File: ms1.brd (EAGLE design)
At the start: 160 x 100 mm, 145 parts, among them IC1 MAX3232EUE, IC2 MAX3380EEUP, J1 POWERPOLE_POWER25A, J10 Radio, J11 A3, J12 A4, J13 A5, J14 A6, J15 A7, J16 D1, J17 D2, J18 D3, J19 D4, J2 ON, J20 D5, J21 D6, J22 D7, J3 LED-EN, J4 RS232, J5 RS485, J6 A1, J7 I2C, J8 A2, J9 TTL_SERIAL, Q1 DMG6602SVT, Q2 DMG6602SVT, Q3 DMG6602SVT, Q4 DMG6602SVT, U1 LT1934ES6TRMPBF, U2 LT1934ES6TRMPBF, U3 DS3231SN, U4 ISL3179EIBZ, X1 KUSBVX-BS1N

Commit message: a little more routing
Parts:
- moved AGND 377.8 mm to (166.1, -11.8)
- moved BATV_B 276.8 mm to (63.8, 95.6)
- moved U$1 248.6 mm to (51.3, 80.5)
- moved U3 203.2 mm to (35.7, 59.9), flipped to the bottom, turned to 180 degrees
- moved U$4 42.3 mm to (124.8, 36.1)
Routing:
- net VBAT_B: track 0.00 -> 38.7 mm
- net GND: track 17.5 -> 17.6 mm, vias 3 -> 4

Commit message: power supplies mostly routed
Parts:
- moved Q4 253.2 mm to (111.5, 77.7), turned to 180 degrees
- moved R5 234.5 mm to (79.0, 92.8)
- moved L3 233.0 mm to (90.6, 87.5)
- moved C12 230.0 mm to (145.0, 83.9), turned to 270 degrees
- moved R31 223.4 mm to (149.5, 89.8), turned to 180 degrees
- moved 5V 222.3 mm to (149.9, 93.6)
- moved C11 216.4 mm to (127.6, 80.4), turned to 90 degrees
- moved R11 212.3 mm to (119.4, 80.9), turned to 180 degrees
- moved L6 207.7 mm to (143.3, 93.6)
- moved Q2 202.7 mm to (117.9, 84.6)
- moved R6 202.6 mm to (75.6, 89.3), turned to 90 degrees
- moved R9 200.8 mm to (116.5, 83.9), turned to 270 degrees
- moved U2 200.8 mm to (124.3, 88.3), turned to 270 degrees
- moved C8 200.1 mm to (121.2, 87.9), turned to 90 degrees
- moved R23 199.4 mm to (123.8, 94.0)
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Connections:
- net ADC_3V3 renamed VCC-3V
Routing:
- net SENSE_3V3: track 0.00 -> 298.2 mm, vias 0 -> 1
- net SENSE_5V: track 0.00 -> 275.8 mm
- net VCC: track 12.3 -> 148.3 mm
- net N$107: track 0.00 -> 39.8 mm
- net N$6: track 0.00 -> 36.0 mm
- net N$13: track 0.00 -> 16.7 mm
- net N$14: track 0.00 -> 15.1 mm
- net VCC_3V3: track 37.7 -> 52.2 mm
- net N$78: track 0.00 -> 13.8 mm
- net SENSE_EN: track 0.00 -> 12.1 mm, vias 0 -> 2
- net GND: track 17.6 -> 29.6 mm, vias 4 -> 7
- net N$5: track 0.00 -> 10.4 mm
- net N$3: track 0.00 -> 10.1 mm
- net N$118: track 0.00 -> 7.12 mm
- net N$117: track 0.00 -> 6.64 mm
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- added copper zone on layer 1, net GND

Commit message: serial stuff laid out
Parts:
- added C26: 100nF, resistor:C0805
- moved VCC_S 244.9 mm to (106.2, 77.9)
- moved VCC 215.5 mm to (71.9, 94.4)
- moved C23 203.5 mm to (-218.8, 102.7)
- moved C14 186.6 mm to (-219.8, 79.0), turned to 180 degrees
- moved C19 149.9 mm to (-198.6, 104.1), turned to 90 degrees
- moved C13 131.2 mm to (90.3, 144.4), flipped to the bottom, turned to 90 degrees
- moved R32 121.1 mm to (-219.7, 76.6)
- moved U3 89.3 mm to (89.0, 131.6)
- moved C22 82.3 mm to (-220.2, 111.9), turned to 180 degrees
- moved C18 78.2 mm to (-213.4, 110.5), turned to 270 degrees
- moved C20 74.0 mm to (-193.3, 103.1)
- moved IC2 69.1 mm to (-219.1, 107.4), turned to 90 degrees
- moved C17 68.9 mm to (-213.4, 104.8), turned to 270 degrees
- moved C21 64.3 mm to (-193.3, 111.3), turned to 180 degrees
- moved U4 58.4 mm to (-220.1, 72.3)
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- renumbered VCC_3V1 to VCC_3V
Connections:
- net GND: now also C26.2
- net VCC_3V3: now also C26.1
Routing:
- net SPI_CLK: track 33.4 -> 111.0 mm, vias 0 -> 1
- net SPI_SIMO: track 38.0 -> 109.3 mm, vias 0 -> 1
- net SPI_SOMI: track 43.1 -> 105.5 mm, vias 0 -> 2
- net SENSE_3V3: track 298.2 -> 308.8 mm
- net N$10: track 0.00 -> 6.55 mm
- net N$84: track 0.00 -> 6.42 mm
- net N$83: track 0.00 -> 6.34 mm
- net N$59: track 0.00 -> 6.04 mm
- net N$82: track 0.00 -> 4.75 mm
- net N$85: track 0.00 -> 4.58 mm
- net N$87: track 0.00 -> 4.22 mm
- net N$80: track 0.00 -> 3.84 mm
- net N$8: track 0.00 -> 3.69 mm
- net N$86: track 0.00 -> 3.54 mm
- net N$9: track 0.00 -> 3.50 mm
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
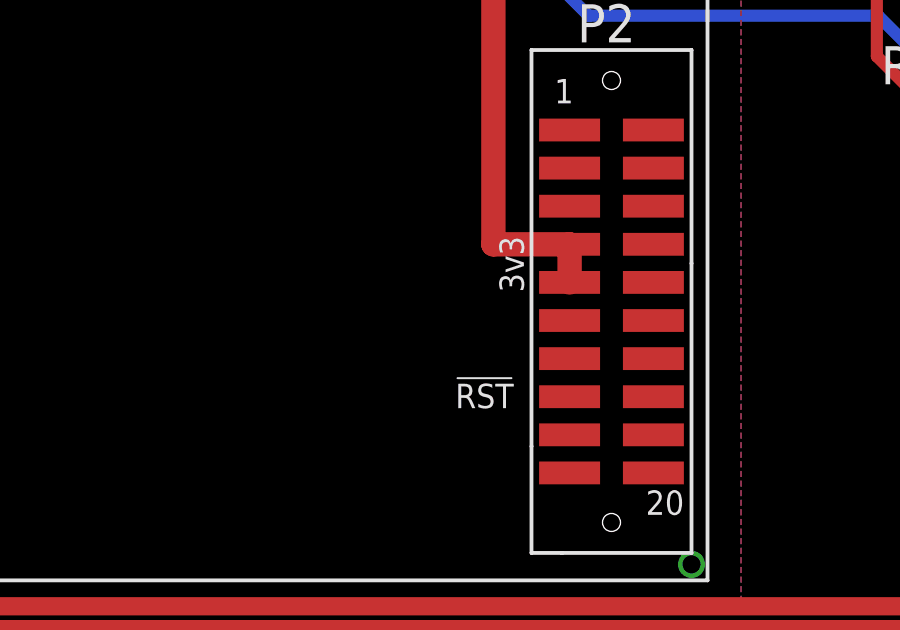
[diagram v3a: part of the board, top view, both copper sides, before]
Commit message: added pullup to !RESET on CC1120
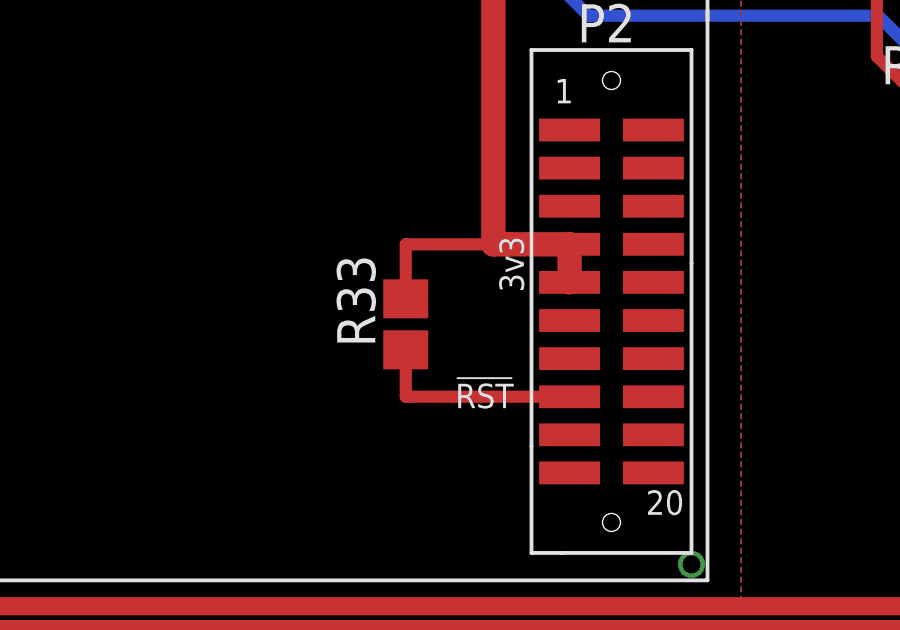
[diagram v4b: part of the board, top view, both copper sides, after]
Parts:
- added R33: 1K, resistor:R0805
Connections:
- new net N$17: R33.1, U$3.RESET
- net RADIO_3V3: now also R33.2
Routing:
- net N$17: track 0.00 -> 7.02 mm
- net RADIO_3V3: track 69.6 -> 74.8 mm
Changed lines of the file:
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@@
 <attribute name="NAME" x="-227.711" y="105.41" size="1.27" layer="25" rot="R270"/>
 </element>
+<element name="R33" library="resistor" package="R0805" value="1K" x="37.719" y="10.668" rot="R90"/>
 </elements>
 <signals>
@@
 <contactref element="U$3" pad="3V3-2"/>
 <wire x1="43.18" y1="12.065" x2="43.18" y2="13.335" width="0.8128" layer="1"/>
-<wire x1="43.18" y1="13.335" x2="40.64" y2="13.335" width="0.8128" layer="1"/>
+<wire x1="43.18" y1="13.335" x2="41.148" y2="13.335" width="0.8128" layer="1"/>
+<wire x1="41.148" y1="13.335" x2="40.64" y2="13.335" width="0.8128" layer="1"/>
 <wire x1="40.64" y1="13.335" x2="40.64" y2="29.21" width="0.8128" layer="1"/>
 <wire x1="40.64" y1="29.21" x2="44.196" y2="29.21" width="0.8128" layer="1"/>
@@
 <wire x1="40.64" y1="32.0675" x2="40.64" y2="29.21" width="0.8128" layer="1"/>
 <wire x1="7.9375" y1="35.98" x2="7.9375" y2="32.0675" width="0.4064" layer="1"/>
+<contactref element="R33" pad="2"/>
+<wire x1="37.719" y1="11.518" x2="37.719" y2="13.335" width="0.4064" layer="1"/>
+<wire x1="37.719" y1="13.335" x2="41.148" y2="13.335" width="0.4064" layer="1"/>
 </signal>
 <signal name="N$13">
@@
 <contactref element="U$2" pad="A4" route="any" routetag="G$1.VCC-3V"/>
 </signal>
+<signal name="N$17">
+<contactref element="U$3" pad="RESET"/>
+<contactref element="R33" pad="1"/>
+<wire x1="43.18" y1="8.255" x2="37.719" y2="8.255" width="0.4064" layer="1"/>
+<wire x1="37.719" y1="8.255" x2="37.719" y2="9.818" width="0.4064" layer="1"/>
+</signal>
 </signals>

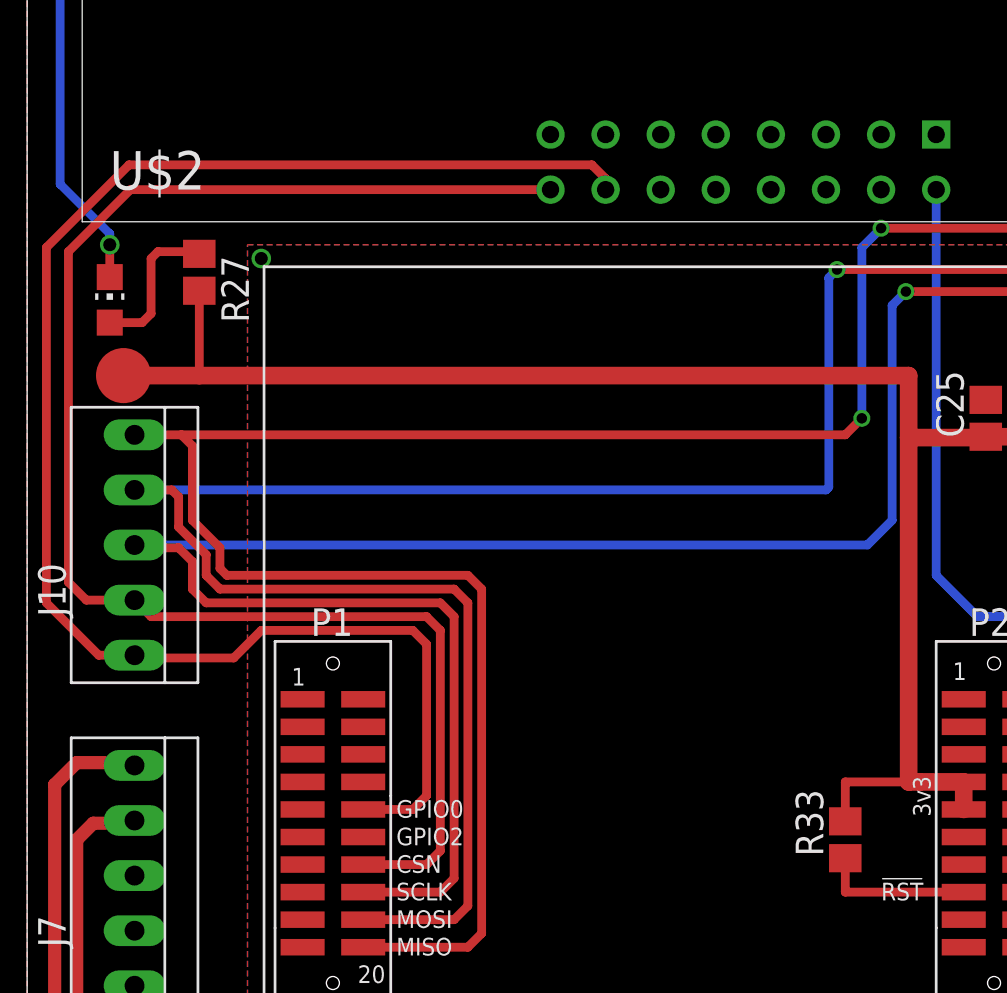
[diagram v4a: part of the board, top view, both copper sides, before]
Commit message: added reset link from cc1120 to msp
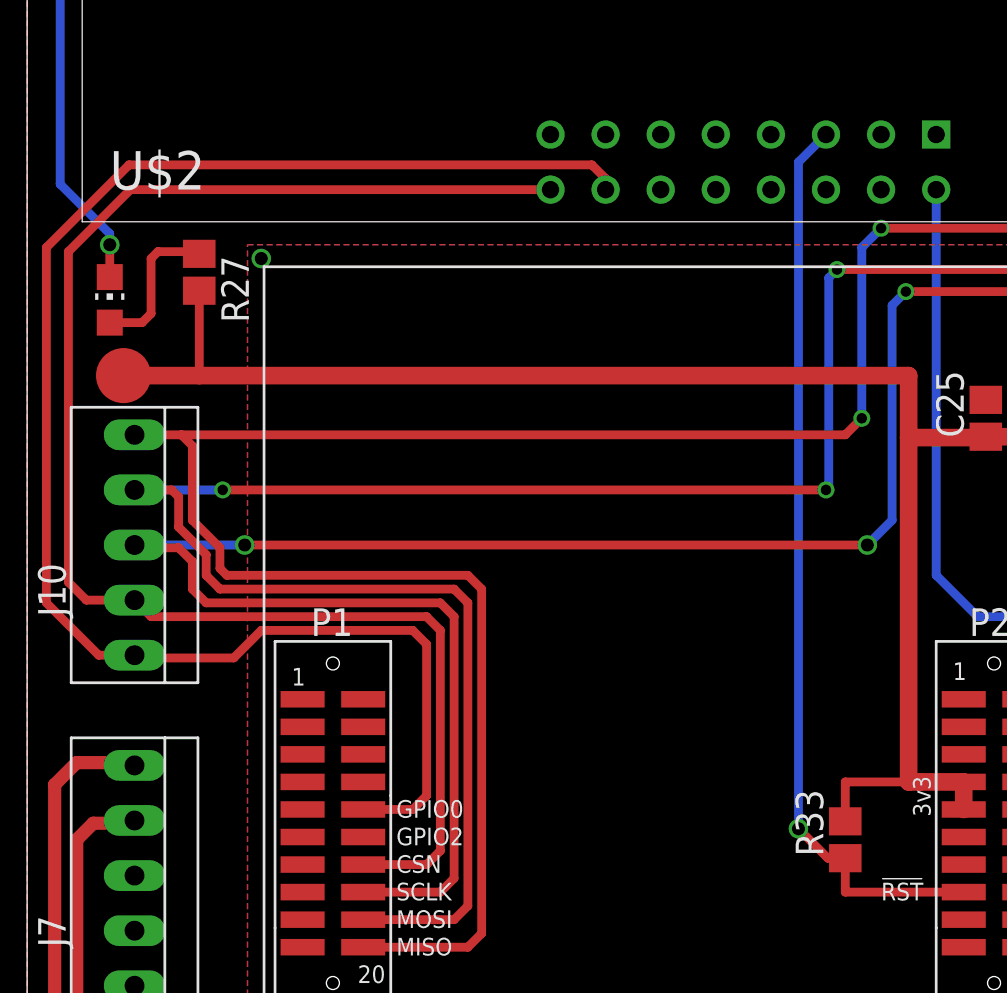
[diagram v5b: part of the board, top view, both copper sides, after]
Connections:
- removed net N$17: R33.1, U$3.RESET
- new net RADIO_!RST: R33.1, U$2.C43, U$3.RESET
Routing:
- net RADIO_!RST: track 0.00 -> 42.3 mm, vias 0 -> 1
- net N$17: track 7.02 -> 0.00 mm
- net SPI_CLK: vias 1 -> 3
- net SPI_SIMO: vias 1 -> 3
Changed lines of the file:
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@@
 <wire x1="6.985" y1="24.13" x2="5.08" y2="24.13" width="0.4064" layer="1"/>
 <wire x1="5.08" y1="24.13" x2="4.953" y2="24.257" width="0.4064" layer="1"/>
-<wire x1="4.953" y1="24.257" x2="38.735" y2="24.257" width="0.4064" layer="16"/>
 <wire x1="38.735" y1="24.257" x2="39.878" y2="25.4" width="0.4064" layer="16"/>
 <wire x1="39.878" y1="25.4" x2="39.878" y2="35.306" width="0.4064" layer="16"/>
@@
 <wire x1="58.801" y1="48.26" x2="57.15" y2="48.26" width="0.4064" layer="1"/>
 <wire x1="59.817" y1="47.244" x2="124.841" y2="46.228" width="0" layer="19" extent="1-1"/>
+<via x="38.735" y="24.257" extent="1-16" drill="0.6"/>
+<wire x1="38.735" y1="24.257" x2="10.033" y2="24.257" width="0.4064" layer="1"/>
+<via x="10.033" y="24.257" extent="1-16" drill="0.6"/>
+<wire x1="10.033" y1="24.257" x2="4.953" y2="24.257" width="0.4064" layer="16"/>
 </signal>
 <signal name="SPI_SIMO">
@@
 <wire x1="58.674" y1="39.751" x2="58.674" y2="44.196" width="0.4064" layer="1"/>
 <wire x1="58.674" y1="44.196" x2="57.15" y2="45.72" width="0.4064" layer="1"/>
-<wire x1="36.83" y1="26.797" x2="4.953" y2="26.797" width="0.4064" layer="16"/>
 <wire x1="58.674" y1="44.196" x2="135.001" y2="46.228" width="0" layer="19" extent="1-1"/>
+<via x="36.83" y="26.797" extent="1-16" drill="0.4826"/>
+<wire x1="36.83" y1="26.797" x2="9.017" y2="26.797" width="0.4064" layer="1"/>
+<via x="9.017" y="26.797" extent="1-16" drill="0.4826"/>
+<wire x1="9.017" y1="26.797" x2="4.953" y2="26.797" width="0.4064" layer="16"/>
 </signal>
 <signal name="SPI_SOMI">
@@
 <contactref element="U$2" pad="A4" route="any" routetag="G$1.VCC-3V"/>
 </signal>
-<signal name="N$17">
+<signal name="RADIO_!RST">
+<contactref element="U$2" pad="C43"/>
 <contactref element="U$3" pad="RESET"/>
 <contactref element="R33" pad="1"/>
 <wire x1="43.18" y1="8.255" x2="37.719" y2="8.255" width="0.4064" layer="1"/>
 <wire x1="37.719" y1="8.255" x2="37.719" y2="9.818" width="0.4064" layer="1"/>
+<wire x1="36.83" y1="43.18" x2="35.56" y2="41.91" width="0.4064" layer="16"/>
+<wire x1="35.56" y1="41.91" x2="35.56" y2="11.176" width="0.4064" layer="16"/>
+<via x="35.56" y="11.176" extent="1-16" drill="0.6"/>
+<wire x1="35.56" y1="11.176" x2="36.918" y2="9.818" width="0.4064" layer="1"/>
+<wire x1="36.918" y1="9.818" x2="37.719" y2="9.818" width="0.4064" layer="1"/>
 </signal>
 </signals>

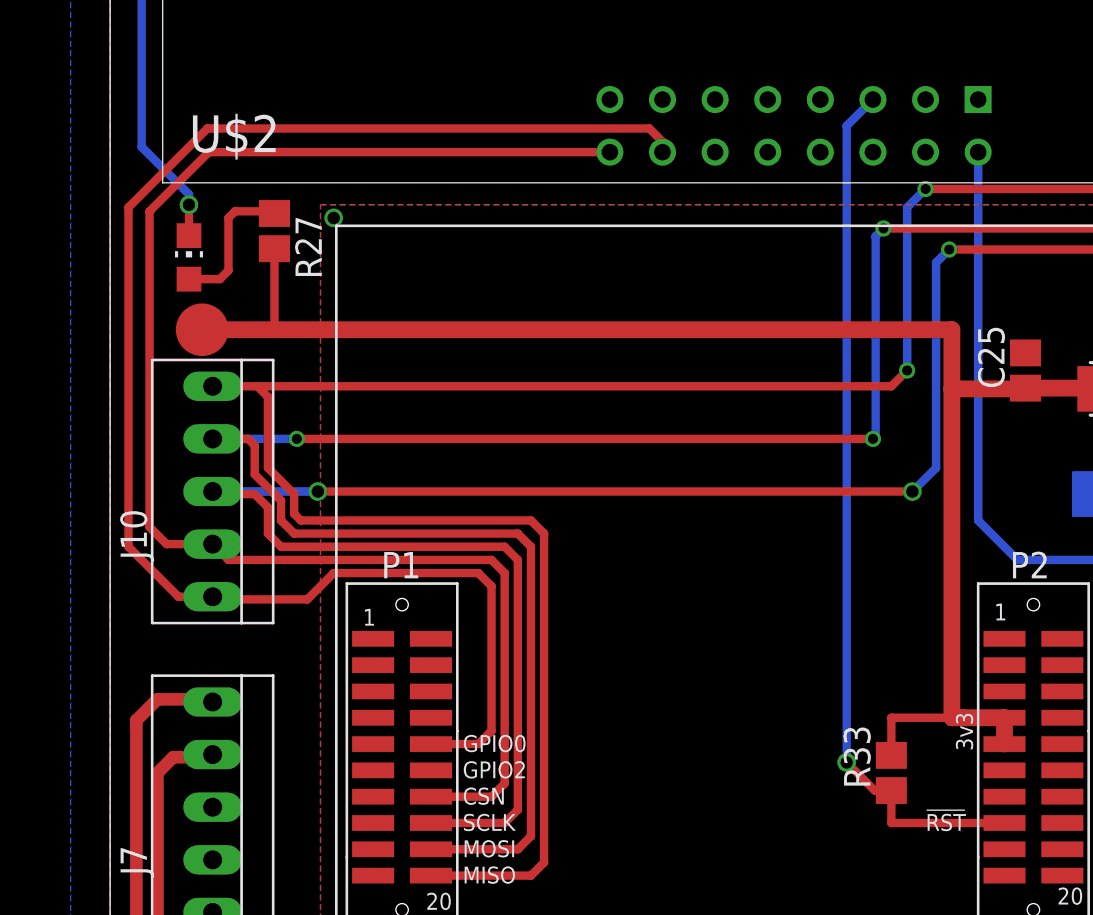
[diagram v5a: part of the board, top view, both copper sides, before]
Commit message: cc1120 wiring matches test harness
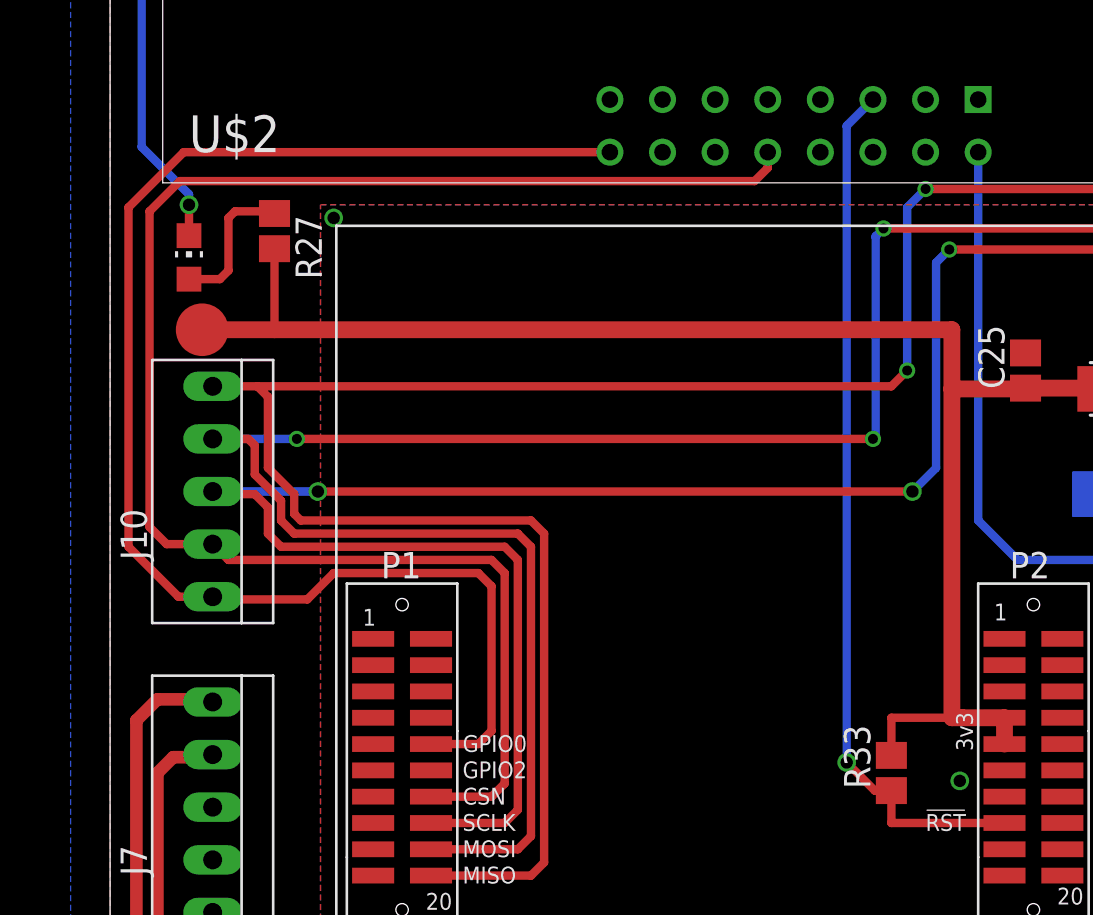
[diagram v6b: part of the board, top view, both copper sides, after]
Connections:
- net DIO_7: no longer U$2.C48
- net RADIO_CSN: now also U$2.C48; no longer U$2.C54
- net RADIO_INT: now also U$2.C54; no longer U$2.C52
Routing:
- net RADIO_CSN: track 70.7 -> 78.8 mm
- net RADIO_INT: track 74.6 -> 70.8 mm
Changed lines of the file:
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@@
 <signal name="DIO_7">
 <contactref element="R18" pad="2"/>
-<contactref element="U$2" pad="C48"/>
 <contactref element="JP15" pad="3"/>
-<wire x1="31.75" y1="40.64" x2="38.1" y2="133.35" width="0" layer="19" extent="1-1"/>
 <wire x1="-171.45" y1="136.74" x2="38.1" y2="133.35" width="0" layer="19" extent="1-1"/>
 </signal>
@@
 <via x="48.514" y="34.163" extent="1-16" drill="0.6" shape="square"/>
 <via x="10.795" y="37.465" extent="1-16" drill="0.6" shape="square"/>
+<via x="41.021" y="10.287" extent="1-16" drill="0.6" shape="square"/>
 </signal>
 <signal name="N$24">
@@
 <wire x1="59.817" y1="47.244" x2="58.801" y2="48.26" width="0.4064" layer="1"/>
 <wire x1="58.801" y1="48.26" x2="57.15" y2="48.26" width="0.4064" layer="1"/>
-<wire x1="59.817" y1="47.244" x2="124.841" y2="46.228" width="0" layer="19" extent="1-1"/>
 <via x="38.735" y="24.257" extent="1-16" drill="0.6"/>
 <wire x1="38.735" y1="24.257" x2="10.033" y2="24.257" width="0.4064" layer="1"/>
 <via x="10.033" y="24.257" extent="1-16" drill="0.6"/>
 <wire x1="10.033" y1="24.257" x2="4.953" y2="24.257" width="0.4064" layer="16"/>
+<wire x1="59.817" y1="47.244" x2="124.841" y2="46.228" width="0" layer="19" extent="1-1"/>
 </signal>
 <signal name="SPI_SIMO">
@@
 <wire x1="58.674" y1="39.751" x2="58.674" y2="44.196" width="0.4064" layer="1"/>
 <wire x1="58.674" y1="44.196" x2="57.15" y2="45.72" width="0.4064" layer="1"/>
-<wire x1="58.674" y1="44.196" x2="135.001" y2="46.228" width="0" layer="19" extent="1-1"/>
 <via x="36.83" y="26.797" extent="1-16" drill="0.4826"/>
 <wire x1="36.83" y1="26.797" x2="9.017" y2="26.797" width="0.4064" layer="1"/>
 <via x="9.017" y="26.797" extent="1-16" drill="0.4826"/>
 <wire x1="9.017" y1="26.797" x2="4.953" y2="26.797" width="0.4064" layer="16"/>
+<wire x1="58.674" y1="44.196" x2="135.001" y2="46.228" width="0" layer="19" extent="1-1"/>
 </signal>
 <signal name="SPI_SOMI">
@@
 <signal name="RADIO_CSN">
 <contactref element="U$3" pad="CSN"/>
-<contactref element="U$2" pad="C54"/>
 <contactref element="J10" pad="2"/>
 <wire x1="15.494" y1="9.525" x2="18.415" y2="9.525" width="0.4064" layer="1"/>
@@
 <wire x1="2.7305" y1="21.717" x2="1.905" y2="22.5425" width="0.4064" layer="1"/>
 <wire x1="1.905" y1="22.5425" x2="1.905" y2="37.7825" width="0.4064" layer="1"/>
-<wire x1="1.905" y1="37.7825" x2="4.7625" y2="40.64" width="0.4064" layer="1"/>
-<wire x1="4.7625" y1="40.64" x2="24.13" y2="40.64" width="0.4064" layer="1"/>
+<wire x1="1.905" y1="37.7825" x2="3.3655" y2="39.243" width="0.4064" layer="1"/>
+<contactref element="U$2" pad="C48"/>
+<wire x1="31.75" y1="40.64" x2="31.75" y2="39.878" width="0.4064" layer="1"/>
+<wire x1="31.75" y1="39.878" x2="31.115" y2="39.243" width="0.4064" layer="1"/>
+<wire x1="31.115" y1="39.243" x2="3.3655" y2="39.243" width="0.4064" layer="1"/>
 </signal>
 <signal name="USB_VCC">
@@
 </signal>
 <signal name="RADIO_INT">
-<contactref element="U$2" pad="C52"/>
 <contactref element="U$3" pad="GPIO0"/>
 <contactref element="J10" pad="1"/>
@@
 <wire x1="5.461" y1="19.05" x2="5.08" y2="19.05" width="0.4064" layer="1"/>
 <wire x1="5.08" y1="19.05" x2="4.953" y2="19.177" width="0.4064" layer="1"/>
-<wire x1="26.67" y1="40.64" x2="26.67" y2="41.148" width="0.4064" layer="1"/>
-<wire x1="26.67" y1="41.148" x2="26.035" y2="41.783" width="0.4064" layer="1"/>
-<wire x1="26.035" y1="41.783" x2="4.699" y2="41.783" width="0.4064" layer="1"/>
-<wire x1="4.699" y1="41.783" x2="0.889" y2="37.973" width="0.4064" layer="1"/>
 <wire x1="0.889" y1="37.973" x2="0.889" y2="21.59" width="0.4064" layer="1"/>
 <wire x1="0.889" y1="21.59" x2="3.302" y2="19.177" width="0.4064" layer="1"/>
 <wire x1="3.302" y1="19.177" x2="5.334" y2="19.177" width="0.4064" layer="1"/>
 <wire x1="5.334" y1="19.177" x2="5.461" y2="19.05" width="0.4064" layer="1"/>
+<contactref element="U$2" pad="C54"/>
+<wire x1="24.13" y1="40.64" x2="3.556" y2="40.64" width="0.4064" layer="1"/>
+<wire x1="3.556" y1="40.64" x2="0.889" y2="37.973" width="0.4064" layer="1"/>
 </signal>
 <signal name="ADC_1">
